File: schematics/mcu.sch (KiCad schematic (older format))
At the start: 16 parts

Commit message: split into 2 sheets + drc
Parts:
- added U2: TPD4E002, symbol TPD4E002
- gave numbers to parts that had none: 16
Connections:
- wire segments 77 -> 66
- no-connect marks 0 -> 9

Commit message: added pullups for I2C and alert
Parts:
- removed L1, L2, L3: 6.5uH, symbol L_Core_Iron_Small
- removed P4: RESET, symbol CONN_01X02
- added L1: 100R, symbol Ferrite_Bead_Small
- added SW1: RESET, symbol SW_Push_Dual
- C1, C2, C3: footprint (none) -> Capacitors_SMD:C_0805_HandSoldering
- D1: footprint (none) -> LEDs:LED_0805
- P1, P2, P3: footprint (none) -> Pin_Headers:Pin_Header_Straight_1x04_Pitch2.54mm
- P5: footprint (none) -> Connect:USB_Micro-B
- R6: renamed from R1; footprint (none) -> Resistors_SMD:R_0805_HandSoldering
- R7: renamed from R2; footprint (none) -> Resistors_SMD:R_0805_HandSoldering
- R8: renamed from R3; footprint (none) -> Resistors_SMD:R_0805_HandSoldering
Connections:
- wire segments 66 -> 67
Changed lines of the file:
@@
 F 0 "P5" H 7875 2825 50  0000 C CNN
 F 1 "USB_OTG" H 7550 3150 50  0000 C CNN
-F 2 "" V 7500 2850 50  0000 C CNN
+F 2 "Connect:USB_Micro-B" V 7500 2850 50  0001 C CNN
 F 3 "" V 7500 2850 50  0000 C CNN
 	1    7550 2950
@@
 F 0 "P2" H 3550 2700 50  0000 C CNN
 F 1 "UART Conn" V 3650 2450 50  0000 C CNN
-F 2 "" H 3550 2450 50  0000 C CNN
+F 2 "Pin_Headers:Pin_Header_Straight_1x04_Pitch2.54mm" H 3550 2450 50  0001 C CNN
 F 3 "" H 3550 2450 50  0000 C CNN
 	1    3550 2450
@@
 F 0 "P3" H 3550 4500 50  0000 C CNN
 F 1 "Debug Conn" V 3650 4250 50  0000 C CNN
-F 2 "" H 3550 4250 50  0000 C CNN
+F 2 "Pin_Headers:Pin_Header_Straight_1x04_Pitch2.54mm" H 3550 4250 50  0001 C CNN
 F 3 "" H 3550 4250 50  0000 C CNN
 	1    3550 4250
@@
 F 0 "P1" H 2500 3550 50  0000 C CNN
 F 1 "I2C Conn" V 2600 3300 50  0000 C CNN
-F 2 "" H 2500 3300 50  0000 C CNN
+F 2 "Pin_Headers:Pin_Header_Straight_1x04_Pitch2.54mm" H 2500 3300 50  0001 C CNN
 F 3 "" H 2500 3300 50  0000 C CNN
 	1    2500 3300
@@
 F 0 "U1" H 5450 4050 60  0000 C CNN
 F 1 "EFM32HG309" H 6000 5025 39  0000 C CNN
-F 2 "" H 5350 4450 60  0000 C CNN
+F 2 "" H 5350 4450 60  0001 C CNN
 F 3 "" H 5350 4450 60  0000 C CNN
 	1    5450 4150
@@
 $EndComp
 $Comp
-L R_Small R1
+L R_Small R6
 U 1 1 5881A46F
 P 6550 2850
-F 0 "R1" V 6550 2800 50  0000 L CNN
+F 0 "R6" V 6550 2800 50  0000 L CNN
 F 1 "15R" V 6500 2950 50  0000 L CNN
-F 2 "" H 6550 2850 50  0000 C CNN
+F 2 "Resistors_SMD:R_0805_HandSoldering" H 6550 2850 50  0001 C CNN
 F 3 "" H 6550 2850 50  0000 C CNN
 	1    6550 2850
@@
 $EndComp
 $Comp
-L R_Small R2
+L R_Small R7
 U 1 1 5881A476
 P 6550 2950
-F 0 "R2" V 6550 2900 50  0000 L CNN
+F 0 "R7" V 6550 2900 50  0000 L CNN
 F 1 "15R" V 6600 3050 50  0000 L CNN
-F 2 "" H 6550 2950 50  0000 C CNN
+F 2 "Resistors_SMD:R_0805_HandSoldering" H 6550 2950 50  0001 C CNN
 F 3 "" H 6550 2950 50  0000 C CNN
 	1    6550 2950
@@
 F 0 "C3" H 6760 4120 50  0000 L CNN
 F 1 "1uF" H 6800 4000 50  0000 L CNN
-F 2 "" H 6750 4050 50  0000 C CNN
+F 2 "Capacitors_SMD:C_0805_HandSoldering" H 6750 4050 50  0001 C CNN
 F 3 "" H 6750 4050 50  0000 C CNN
 	1    6750 4050
@@
 F 0 "C2" H 6560 4120 50  0000 L CNN
 F 1 "1uF" H 6550 4000 50  0000 L CNN
-F 2 "" H 6550 4050 50  0000 C CNN
+F 2 "Capacitors_SMD:C_0805_HandSoldering" H 6550 4050 50  0001 C CNN
 F 3 "" H 6550 4050 50  0000 C CNN
 	1    6550 4050
@@
 F 0 "D1" H 7050 3500 50  0000 C CNN
 F 1 "LED" V 7150 3300 50  0000 C CNN
-F 2 "" H 7050 3400 50  0000 C CNN
+F 2 "LEDs:LED_0805" H 7050 3400 50  0001 C CNN
 F 3 "" H 7050 3400 50  0000 C CNN
 	1    7050 3400
@@
 $EndComp
 $Comp
-L R_Small R3
+L R_Small R8
 U 1 1 5881A4BE
 P 7050 3650
-F 0 "R3" H 7100 3650 50  0000 L CNN
+F 0 "R8" H 7100 3650 50  0000 L CNN
 F 1 "100R" H 6800 3650 50  0000 L CNN
-F 2 "" H 7050 3650 50  0000 C CNN
+F 2 "Resistors_SMD:R_0805_HandSoldering" H 7050 3650 50  0001 C CNN
 F 3 "" H 7050 3650 50  0000 C CNN
 	1    7050 3650
@@
 $EndComp
 $Comp
-L CONN_01X02 P4
-U 1 1 5881A4C5
-P 4950 4300
-F 0 "P4" H 4950 4450 50  0000 C CNN
-F 1 "RESET" V 5050 4300 50  0000 C CNN
-F 2 "" H 4950 4300 50  0000 C CNN
-F 3 "" H 4950 4300 50  0000 C CNN
-	1    4950 4300
-	-1   0    0    1
-$EndComp
-$Comp
 L GND #PWR09
 U 1 1 5881A4CC
-P 5150 4450
-F 0 "#PWR09" H 5150 4200 50  0001 C CNN
-F 1 "GND" H 5150 4300 50  0000 C CNN
-F 2 "" H 5150 4450 50  0000 C CNN
-F 3 "" H 5150 4450 50  0000 C CNN
-	1    5150 4450
+P 5150 4700
+F 0 "#PWR09" H 5150 4450 50  0001 C CNN
+F 1 "GND" H 5150 4550 50  0000 C CNN
+F 2 "" H 5150 4700 50  0000 C CNN
+F 3 "" H 5150 4700 50  0000 C CNN
+	1    5150 4700
 	1    0    0    -1
 $EndComp
@@
 F 0 "C1" H 6100 2350 50  0000 L CNN
 F 1 "4.7uF" H 6050 2250 50  0000 L CNN
-F 2 "" H 6300 2350 50  0000 C CNN
+F 2 "Capacitors_SMD:C_0805_HandSoldering" H 6300 2350 50  0001 C CNN
 F 3 "" H 6300 2350 50  0000 C CNN
 	1    6300 2350
@@
 Text Label 4450 2600 0    60   ~ 0
 UART_RX
-$Comp
-L L_Core_Iron_Small L3
-U 1 1 5881A52A
-P 7650 3450
-F 0 "L3" H 7700 3490 50  0000 L CNN
-F 1 "6.5uH" H 7700 3400 50  0000 L CNN
-F 2 "" H 7650 3450 50  0000 C CNN
-F 3 "" H 7650 3450 50  0000 C CNN
-	1    7650 3450
-	1    0    0    -1
-$EndComp
-$Comp
-L L_Core_Iron_Small L2
-U 1 1 5881A531
-P 7250 3450
-F 0 "L2" H 7300 3490 50  0000 L CNN
-F 1 "6.5uH" H 7300 3400 50  0000 L CNN
-F 2 "" H 7250 3450 50  0000 C CNN
-F 3 "" H 7250 3450 50  0000 C CNN
-	1    7250 3450
-	1    0    0    -1
-$EndComp
-$Comp
-L L_Core_Iron_Small L1
-U 1 1 5881A53A
-P 7100 2750
-F 0 "L1" H 7150 2790 50  0000 L CNN
-F 1 "6.5uH" H 7150 2700 50  0000 L CNN
-F 2 "" H 7100 2750 50  0000 C CNN
-F 3 "" H 7100 2750 50  0000 C CNN
-	1    7100 2750
-	0    -1   -1   0
-$EndComp
 Text HLabel 3100 3000 1    60   Input ~ 0
 I2C0-SDA
@@
 Wire Wire Line
 	5150 4250 5150 4050
-Wire Wire Line
-	5150 4350 5150 4450
 Connection ~ 7250 3850
 Wire Wire Line
-	7050 3850 7650 3850
+	7050 3850 7250 3850
 Wire Wire Line
 	7050 3750 7050 3850
 Connection ~ 6750 3250
 Wire Wire Line
-	7250 3550 7250 4250
+	7250 3150 7250 4250
 Wire Wire Line
 	6450 2850 6450 2850
@@
 Wire Wire Line
 	4350 3450 5150 3450
-Wire Wire Line
-	7250 3150 7250 3350
-Wire Wire Line
-	7650 3850 7650 3550
 Wire Wire Line
 	7250 2750 7200 2750
@@
 $EndComp
 Connection ~ 7250 4050
+$Comp
+L SW_Push_Dual SW1
+U 1 1 588332AE
+P 5150 4450
+F 0 "SW1" H 5200 4550 50  0000 L CNN
+F 1 "RESET" H 5150 4180 50  0000 C CNN
+F 2 "" H 5150 4650 50  0001 C CNN
+F 3 "" H 5150 4650 50  0000 C CNN
+	1    5150 4450
+	0    1    1    0
+$EndComp
+Wire Wire Line
+	5150 4250 4950 4250
+Wire Wire Line
+	4950 4650 5150 4650
+Wire Wire Line
+	5150 4650 5150 4700
+Wire Wire Line
+	7250 3350 7650 3350
+Connection ~ 7250 3350
+$Comp
+L Ferrite_Bead_Small L1
+U 1 1 58834258
+P 7100 2750
+F 0 "L1" V 7150 2800 50  0000 L CNN
+F 1 "100R" V 7000 2650 50  0000 L CNN
+F 2 "" V 7030 2750 50  0001 C CNN
+F 3 "" H 7100 2750 50  0000 C CNN
+	1    7100 2750
+	0    1    1    0
+$EndComp
 $EndSCHEMATC

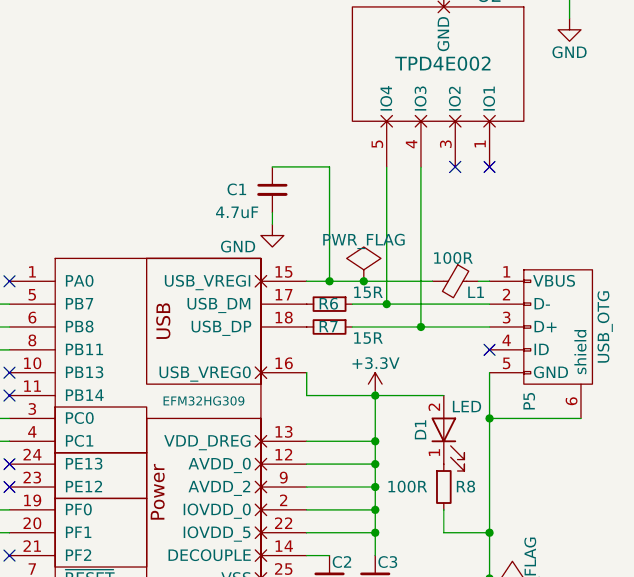
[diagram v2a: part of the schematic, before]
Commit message: added moar decoulping caps
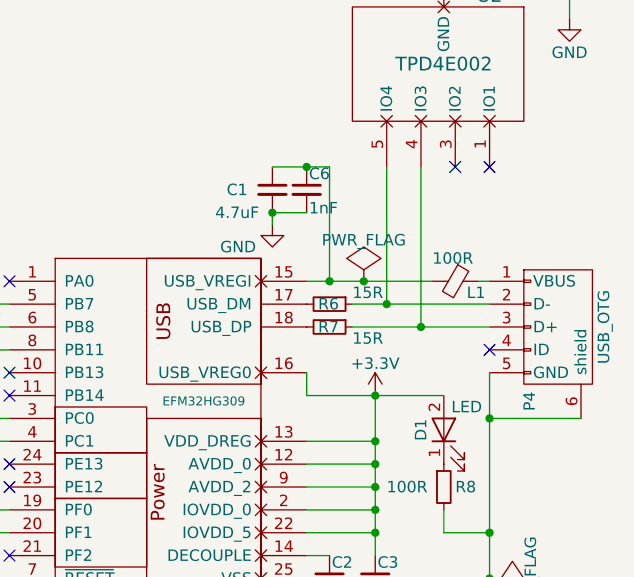
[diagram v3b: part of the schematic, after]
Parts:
- added C6: 1nF, Capacitors_SMD:C_0805_HandSoldering, symbol C_Small
- L1: footprint (none) -> Capacitors_SMD:C_0805_HandSoldering
- renumbered P5 to P4
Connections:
- net GND: now also C6.2
- net at C1.1, L1.2, U1.15 (USB_VREGI): now also C6.1
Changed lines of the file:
@@
 $EndDescr
 $Comp
-L USB_OTG P5
+L USB_OTG P4
 U 1 1 5881A446
 P 7550 2950
-F 0 "P5" H 7875 2825 50  0000 C CNN
+F 0 "P4" H 7875 2825 50  0000 C CNN
 F 1 "USB_OTG" H 7550 3150 50  0000 C CNN
 F 2 "Connect:USB_Micro-B" V 7500 2850 50  0001 C CNN
@@
 F 0 "L1" V 7150 2800 50  0000 L CNN
 F 1 "100R" V 7000 2650 50  0000 L CNN
-F 2 "" V 7030 2750 50  0001 C CNN
+F 2 "Capacitors_SMD:C_0805_HandSoldering" V 7030 2750 50  0001 C CNN
 F 3 "" H 7100 2750 50  0000 C CNN
 	1    7100 2750
 	0    1    1    0
 $EndComp
+$Comp
+L C_Small C6
+U 1 1 58848677
+P 6450 2350
+F 0 "C6" H 6460 2420 50  0000 L CNN
+F 1 "1nF" H 6460 2270 50  0000 L CNN
+F 2 "Capacitors_SMD:C_0805_HandSoldering" H 6450 2350 50  0001 C CNN
+F 3 "" H 6450 2350 50  0000 C CNN
+	1    6450 2350
+	1    0    0    -1
+$EndComp
+Wire Wire Line
+	6300 2450 6450 2450
+Connection ~ 6300 2450
+Connection ~ 6450 2250
 $EndSCHEMATC

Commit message: first layout
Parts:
- removed SW1: RESET, symbol SW_Push_Dual
- added SW1: SW_Push, draw:Tact, symbol SW_Push
- U1: footprint (none) -> Housings_DFN_QFN:QFN-24-1EP_5x5mm_Pitch0.65mm
- U2: footprint (none) -> TO_SOT_Packages_SMD:SOT-553
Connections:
- net GND: now also SW1.2
- net at U1.7 (~RESET): now also SW1.1
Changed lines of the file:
@@
 F 0 "U1" H 5450 4050 60  0000 C CNN
 F 1 "EFM32HG309" H 6000 5025 39  0000 C CNN
-F 2 "" H 5350 4450 60  0001 C CNN
+F 2 "Housings_DFN_QFN:QFN-24-1EP_5x5mm_Pitch0.65mm" H 5350 4450 60  0001 C CNN
 F 3 "" H 5350 4450 60  0000 C CNN
 	1    5450 4150
@@
 L GND #PWR09
 U 1 1 5881A4CC
-P 5150 4700
-F 0 "#PWR09" H 5150 4450 50  0001 C CNN
-F 1 "GND" H 5150 4550 50  0000 C CNN
-F 2 "" H 5150 4700 50  0000 C CNN
-F 3 "" H 5150 4700 50  0000 C CNN
-	1    5150 4700
+P 5150 4750
+F 0 "#PWR09" H 5150 4500 50  0001 C CNN
+F 1 "GND" H 5150 4600 50  0000 C CNN
+F 2 "" H 5150 4750 50  0000 C CNN
+F 3 "" H 5150 4750 50  0000 C CNN
+	1    5150 4750
 	1    0    0    -1
 $EndComp
@@
 F 0 "U2" H 7550 1500 60  0000 C CNN
 F 1 "TPD4E002" H 7750 1800 60  0000 C CNN
-F 2 "" H 7400 1550 60  0001 C CNN
+F 2 "TO_SOT_Packages_SMD:SOT-553" H 7400 1550 60  0001 C CNN
 F 3 "" H 7400 1550 60  0001 C CNN
 	1    7400 1550
@@
 Connection ~ 6700 2750
 NoConn ~ 5150 2750
-$Comp
-L PWR_FLAG #FLG013
-U 1 1 588237FC
-P 7250 4050
-F 0 "#FLG013" H 7250 4145 50  0001 C CNN
-F 1 "PWR_FLAG" H 7250 4230 50  0000 C CNN
-F 2 "" H 7250 4050 50  0000 C CNN
-F 3 "" H 7250 4050 50  0000 C CNN
-	1    7250 4050
-	0    1    1    0
-$EndComp
-Connection ~ 7250 4050
-$Comp
-L SW_Push_Dual SW1
-U 1 1 588332AE
-P 5150 4450
-F 0 "SW1" H 5200 4550 50  0000 L CNN
-F 1 "RESET" H 5150 4180 50  0000 C CNN
-F 2 "" H 5150 4650 50  0001 C CNN
-F 3 "" H 5150 4650 50  0000 C CNN
-	1    5150 4450
-	0    1    1    0
-$EndComp
 Wire Wire Line
 	5150 4250 4950 4250
@@
 	4950 4650 5150 4650
 Wire Wire Line
-	5150 4650 5150 4700
+	5150 4650 5150 4750
 Wire Wire Line
 	7250 3350 7650 3350
@@
 Connection ~ 6300 2450
 Connection ~ 6450 2250
+$Comp
+L PWR_FLAG #FLG013
+U 1 1 588E9D77
+P 7250 4000
+F 0 "#FLG013" H 7250 4095 50  0001 C CNN
+F 1 "PWR_FLAG" H 7250 4180 50  0000 C CNN
+F 2 "" H 7250 4000 50  0000 C CNN
+F 3 "" H 7250 4000 50  0000 C CNN
+	1    7250 4000
+	0    1    1    0
+$EndComp
+Connection ~ 7250 4000
+$Comp
+L SW_Push SW1
+U 1 1 588F2FDA
+P 4950 4450
+F 0 "SW1" H 5000 4550 50  0000 L CNN
+F 1 "SW_Push" H 4950 4390 50  0000 C CNN
+F 2 "draw:Tact" H 4950 4650 50  0001 C CNN
+F 3 "" H 4950 4650 50  0000 C CNN
+	1    4950 4450
+	0    1    1    0
+$EndComp
 $EndSCHEMATC

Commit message: first layout
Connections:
- net GND: now also U1.21 (PF2)
- net I2C0-SDA: now also P1.3 (P3); no longer P1.2 (P2)
- net I2C0_SCL: now also P1.2 (P2); no longer P1.3 (P3)
- net at P4.2 (D-), R6.1: now also U2.4 (IO3); no longer U2.5 (IO4)
- net at P4.3 (D+), R7.1: now also U2.5 (IO4); no longer U2.4 (IO3)
- no-connect marks 9 -> 8
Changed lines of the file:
@@
 	1    0    0    -1
 $EndComp
-Text Label 4400 3250 0    60   ~ 0
-I2C0_SDA
 Text Label 4400 3450 0    60   ~ 0
 I2C0_SCL
@@
 Text Label 4450 2600 0    60   ~ 0
 UART_RX
+Text HLabel 2950 3000 1    60   Input ~ 0
+I2C0-SDA
 Text HLabel 3100 3000 1    60   Input ~ 0
-I2C0-SDA
+I2C0_SCL
 Text HLabel 3250 3000 1    60   Input ~ 0
-I2C0_SCL
-Text HLabel 2950 2950 1    60   Input ~ 0
 3.3V
 Text HLabel 2800 2950 1    60   Input ~ 0
@@
 NoConn ~ 5150 3550
 NoConn ~ 5150 3650
-NoConn ~ 5150 3950
 NoConn ~ 7100 2250
 NoConn ~ 7250 2250
-Wire Wire Line
-	6300 2450 6300 2500
-Wire Wire Line
-	7600 1350 7600 1600
-Wire Wire Line
-	7050 1350 7600 1350
-Connection ~ 6950 2950
-Wire Wire Line
-	6950 2250 6950 2950
-Connection ~ 6800 2850
-Wire Wire Line
-	6800 2250 6800 2850
-Wire Wire Line
-	4800 3050 5150 3050
-Connection ~ 2800 3450
-Wire Wire Line
-	2800 2950 2800 3450
-Wire Wire Line
-	5150 4250 5150 4050
-Connection ~ 7250 3850
-Wire Wire Line
-	7050 3850 7250 3850
-Wire Wire Line
-	7050 3750 7050 3850
-Connection ~ 6750 3250
-Wire Wire Line
-	7250 3150 7250 4250
-Wire Wire Line
-	6450 2850 6450 2850
-Wire Wire Line
-	6650 2850 7250 2850
-Wire Wire Line
-	6450 2950 6450 2950
-Wire Wire Line
-	6650 2950 7250 2950
-Wire Wire Line
-	6450 3150 6450 3250
-Wire Wire Line
-	6450 3250 7050 3250
-Wire Wire Line
-	6450 3450 6750 3450
-Wire Wire Line
-	6750 3250 6750 3950
-Wire Wire Line
-	6750 3550 6450 3550
-Connection ~ 6750 3450
-Wire Wire Line
-	6750 3650 6450 3650
-Connection ~ 6750 3550
-Wire Wire Line
-	6750 3750 6450 3750
-Connection ~ 6750 3650
-Wire Wire Line
-	6750 3850 6450 3850
-Connection ~ 6750 3750
-Wire Wire Line
-	6450 4150 6450 4050
-Wire Wire Line
-	6450 4150 7250 4150
-Connection ~ 7250 4150
-Connection ~ 6750 4150
-Connection ~ 6750 3850
-Connection ~ 6550 4150
-Wire Wire Line
-	6450 3950 6550 3950
-Wire Wire Line
-	3750 2600 3850 2600
-Wire Wire Line
-	3850 2600 3850 2700
-Wire Wire Line
-	3750 4400 3850 4400
-Wire Wire Line
-	3850 4400 3850 4450
-Wire Wire Line
-	2700 3150 3850 3150
-Wire Wire Line
-	3850 3150 3850 3100
-Wire Wire Line
-	2700 3450 3850 3450
-Wire Wire Line
-	3850 3450 3850 3550
-Wire Wire Line
-	3750 4100 3850 4100
-Wire Wire Line
-	3850 4100 3850 4000
-Wire Wire Line
-	3850 2300 3750 2300
-Wire Wire Line
-	3850 2200 3850 2300
-Wire Wire Line
-	5150 3750 4150 3750
-Wire Wire Line
-	4150 3750 4150 4200
-Wire Wire Line
-	4150 4200 3750 4200
-Wire Wire Line
-	5150 3850 4250 3850
-Wire Wire Line
-	4250 3850 4250 4300
-Wire Wire Line
-	4250 4300 3750 4300
-Wire Wire Line
-	3750 2500 4950 2500
-Wire Wire Line
-	4950 2500 4950 2950
-Wire Wire Line
-	3750 2400 5050 2400
-Wire Wire Line
-	5050 2400 5050 2850
-Wire Wire Line
-	5050 2850 5150 2850
-Wire Wire Line
-	4950 2950 5150 2950
-Wire Wire Line
-	2700 3250 5000 3250
-Wire Wire Line
-	5000 3250 5000 3350
-Wire Wire Line
-	5000 3350 5150 3350
-Wire Wire Line
-	2700 3350 4350 3350
-Wire Wire Line
-	4350 3350 4350 3450
-Wire Wire Line
-	4350 3450 5150 3450
-Wire Wire Line
-	7250 2750 7200 2750
-Wire Wire Line
-	6300 2250 6550 2250
-Wire Wire Line
-	3100 3000 3100 3250
-Connection ~ 3100 3250
-Wire Wire Line
-	3250 3000 3250 3350
-Connection ~ 3250 3350
-Wire Wire Line
-	2950 2950 2950 3150
-Connection ~ 2950 3150
-Wire Wire Line
-	6450 2750 7000 2750
-Wire Wire Line
-	6550 2250 6550 2750
-Connection ~ 6550 2750
 $Comp
 L PWR_FLAG #FLG012
@@
 	1    0    0    -1
 $EndComp
-Connection ~ 6700 2750
 NoConn ~ 5150 2750
-Wire Wire Line
-	5150 4250 4950 4250
-Wire Wire Line
-	4950 4650 5150 4650
-Wire Wire Line
-	5150 4650 5150 4750
-Wire Wire Line
-	7250 3350 7650 3350
-Connection ~ 7250 3350
 $Comp
 L Ferrite_Bead_Small L1
@@
 	1    0    0    -1
 $EndComp
-Wire Wire Line
-	6300 2450 6450 2450
-Connection ~ 6300 2450
-Connection ~ 6450 2250
 $Comp
 L PWR_FLAG #FLG013
@@
 	0    1    1    0
 $EndComp
-Connection ~ 7250 4000
 $Comp
 L SW_Push SW1
@@
 	0    1    1    0
 $EndComp
+Wire Wire Line
+	6300 2450 6300 2500
+Wire Wire Line
+	7600 1350 7600 1600
+Wire Wire Line
+	7050 1350 7600 1350
+Wire Wire Line
+	4800 3050 5150 3050
+Connection ~ 2800 3450
+Wire Wire Line
+	2800 2950 2800 3450
+Wire Wire Line
+	5150 4250 5150 4050
+Connection ~ 7250 3850
+Wire Wire Line
+	7250 3850 7050 3850
+Wire Wire Line
+	7050 3750 7050 3850
+Connection ~ 6750 3250
+Wire Wire Line
+	7250 3150 7250 4250
+Wire Wire Line
+	6450 2850 6450 2850
+Wire Wire Line
+	6650 2850 7250 2850
+Wire Wire Line
+	6450 2950 6450 2950
+Wire Wire Line
+	6650 2950 7250 2950
+Wire Wire Line
+	6450 3150 6450 3250
+Wire Wire Line
+	6450 3250 7050 3250
+Wire Wire Line
+	6450 3450 6750 3450
+Wire Wire Line
+	6750 3250 6750 3950
+Wire Wire Line
+	6750 3550 6450 3550
+Connection ~ 6750 3450
+Wire Wire Line
+	6750 3650 6450 3650
+Connection ~ 6750 3550
+Wire Wire Line
+	6750 3750 6450 3750
+Connection ~ 6750 3650
+Wire Wire Line
+	6750 3850 6450 3850
+Connection ~ 6750 3750
+Wire Wire Line
+	6450 4150 6450 4050
+Wire Wire Line
+	6450 4150 7250 4150
+Connection ~ 7250 4150
+Connection ~ 6750 4150
+Connection ~ 6750 3850
+Connection ~ 6550 4150
+Wire Wire Line
+	6450 3950 6550 3950
+Wire Wire Line
+	3750 2600 3850 2600
+Wire Wire Line
+	3850 2600 3850 2700
+Wire Wire Line
+	3750 4400 3850 4400
+Wire Wire Line
+	3850 4400 3850 4450
+Wire Wire Line
+	2700 3150 3850 3150
+Wire Wire Line
+	3850 3150 3850 3100
+Wire Wire Line
+	2700 3450 3850 3450
+Wire Wire Line
+	3850 3450 3850 3550
+Wire Wire Line
+	3750 4100 3850 4100
+Wire Wire Line
+	3850 4100 3850 4000
+Wire Wire Line
+	3850 2300 3750 2300
+Wire Wire Line
+	3850 2200 3850 2300
+Wire Wire Line
+	5150 3750 4150 3750
+Wire Wire Line
+	4150 3750 4150 4200
+Wire Wire Line
+	4150 4200 3750 4200
+Wire Wire Line
+	5150 3850 4250 3850
+Wire Wire Line
+	4250 3850 4250 4300
+Wire Wire Line
+	4250 4300 3750 4300
+Wire Wire Line
+	3750 2500 4950 2500
+Wire Wire Line
+	4950 2500 4950 2950
+Wire Wire Line
+	3750 2400 5050 2400
+Wire Wire Line
+	5050 2400 5050 2850
+Wire Wire Line
+	5050 2850 5150 2850
+Wire Wire Line
+	4950 2950 5150 2950
+Wire Wire Line
+	2700 3350 5150 3350
+Wire Wire Line
+	4350 3250 4350 3450
+Wire Wire Line
+	4350 3450 5150 3450
+Wire Wire Line
+	7250 2750 7200 2750
+Wire Wire Line
+	6300 2250 6550 2250
+Wire Wire Line
+	6450 2750 7000 2750
+Wire Wire Line
+	6550 2250 6550 2750
+Connection ~ 6550 2750
+Connection ~ 6700 2750
+Wire Wire Line
+	5150 4250 4950 4250
+Wire Wire Line
+	4950 4650 5150 4650
+Wire Wire Line
+	5150 4650 5150 4750
+Wire Wire Line
+	7250 3350 7650 3350
+Connection ~ 7250 3350
+Wire Wire Line
+	6300 2450 6450 2450
+Connection ~ 6300 2450
+Connection ~ 6450 2250
+Connection ~ 7250 4000
+Text Label 4700 3350 0    60   ~ 0
+I2C0_SDA
+Wire Wire Line
+	2700 3250 4350 3250
+Wire Wire Line
+	2950 3000 2950 3350
+Wire Wire Line
+	3100 3000 3100 3250
+Connection ~ 3100 3250
+Connection ~ 2950 3350
+Wire Wire Line
+	3250 3000 3250 3150
+Connection ~ 3250 3150
+Wire Wire Line
+	6800 2250 6800 2950
+Connection ~ 6800 2950
+Wire Wire Line
+	6950 2250 6950 2850
+Connection ~ 6950 2850
+$Comp
+L GND #PWR?
+U 1 1 58948119
+P 5100 3950
+F 0 "#PWR?" H 5100 3700 50  0001 C CNN
+F 1 "GND" H 5000 3850 50  0000 C CNN
+F 2 "" H 5100 3950 50  0000 C CNN
+F 3 "" H 5100 3950 50  0000 C CNN
+	1    5100 3950
+	1    0    0    -1
+$EndComp
+Wire Wire Line
+	5150 3950 5100 3950
 $EndSCHEMATC

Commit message: updated to work in kicad 5.1
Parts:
- C1, C2, C3, C6: symbol C_Small -> Device:C_Small
- D1: symbol LED -> Device:LED
- L1: symbol Ferrite_Bead_Small -> Device:Ferrite_Bead_Small
- P1, P2, P3: symbol CONN_01X04 -> Connector:Conn_01x04_Male
- P4: symbol USB_OTG -> Connector:USB_OTG
- R6, R7, R8: symbol R_Small -> Device:R_Small
- SW1: symbol SW_Push -> Switch:SW_Push
- U1: symbol EFM32HG309 -> draw:EFM32HG309
- U2: symbol TPD4E002 -> draw:TPD4E002
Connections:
- net +3V3: now also P1.4 (Pin_4), P2.4 (Pin_4), P3.4 (Pin_4); no longer P1.1 (P1), P2.1 (P1), P3.1 (P1)
- net GND: now also P1.1 (Pin_1), P2.1 (Pin_1), P3.1 (Pin_1); no longer P1.4 (P4), P2.4 (P4), P3.4 (P4)
- net I2C0-SDA: now also P1.2 (Pin_2); no longer P1.3 (P3)
- net I2C0_SCL: now also P1.3 (Pin_3); no longer P1.2 (P2)
- net SWD_CLK: now also P3.3 (Pin_3); no longer P3.2 (P2)
- net UART_TX: now also P2.3 (Pin_3); no longer P2.2 (P2)
- net at U1.6 (PB8): now also P2.2 (Pin_2); no longer P2.3 (P3)
- net at U1.20 (PF1): now also P3.2 (Pin_2); no longer P3.3 (P3)
